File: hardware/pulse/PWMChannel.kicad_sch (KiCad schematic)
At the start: 6 parts, among them J201 WAGO-2065, J202 WAGO-2065, Q201 BSC010N04LS

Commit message: Update parts
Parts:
- C201: footprint Capacitor_SMD:C_0603_1608Metric -> V2_Capacitor_SMD:C_0603; symbol Device:C_Small -> V2_Device:C_0603_0u1; Manufacturer (none) -> TDK; Mouser (none) -> 810-CGA3E2X7R1H104MA; Product (none) -> CGA3E2X7R1H104M080AA
- D201: footprint Diode_SMD:D_SOD-123F -> V2_Diode_SMD:D_SOD-123F; Manufacturer (none) -> onsemi; Mouser (none) -> 512-S310FA; Product (none) -> S310FA
- D202: LCSC (none) -> C965555; Manufacturer (none) -> Worldsemi; Product (none) -> WS2812B-2020
- J201, J202: value WAGO-2065 -> WAGO 2065-100; Manufacturer (none) -> WAGO; Product (none) -> 2065-100/998-403
- Q201: Manufacturer (none) -> Infineon Technologies; Mouser (none) -> 726-BSC010N04LS; Product (none) -> BSC010N04LS
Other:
- moved on the sheet: C201, D201, D202, J201, J202, Q201

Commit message: Refresh
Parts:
- Q201: Polarity (none) -> N; Rating (none) -> 40V
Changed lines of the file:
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@@
-			)
-		)
-		(property "Sim.Pin" ""
-			(at 135.89 93.98 90)
-			(effects
-				(font
-					(size 1.27 1.27)
-				)
-				(hide yes)
 			)
 		)
@@
 		(property "Product" "S310FA"
 			(at 123.19 93.98 0)
-			(effects
-				(font
-					(size 1.27 1.27)
-				)
-				(hide yes)
-			)
-		)
-		(property "Sim.Enable" ""
-			(at 135.89 93.98 90)
 			(effects
 				(font
@@
 			)
 		)
-		(property "Sim.Pin" ""
-			(at 123.19 93.98 0)
-			(effects
-				(font
-					(size 1.27 1.27)
-				)
-				(hide yes)
-			)
-		)
 		(property "Manufacturer" "TDK"
 			(at 123.19 109.22 0)
@@
 		(property "Product" "CGA3E2X7R1H104M080AA"
 			(at 123.19 111.76 0)
-			(effects
-				(font
-					(size 1.27 1.27)
-				)
-				(hide yes)
-			)
-		)
-		(property "Sim.Enable" ""
-			(at 123.19 93.98 0)
 			(effects
 				(font
@@
 			)
 		)
-		(property "Sim.Pin" ""
-			(at 120.65 101.6 0)
-			(effects
-				(font
-					(size 1.27 1.27)
-				)
-				(hide yes)
-			)
-		)
 		(property "Product" "BSC010N04LS"
 			(at 120.65 121.92 0)
@@
 			)
 		)
-		(property "Sim.Enable" ""
-			(at 120.65 101.6 0)
+		(property "Rating" "40V"
+			(at 120.65 121.92 0)
+			(effects
+				(font
+					(size 1.27 1.27)
+				)
+				(hide yes)
+			)
+		)
+		(property "Polarity" "N"
+			(at 120.65 119.38 0)
 			(effects
 				(font
@@
 			)
 		)
-		(property "Sim.Pin" ""
-			(at 148.59 130.81 0)
-			(effects
-				(font
-					(size 1.27 1.27)
-				)
-				(hide yes)
-			)
-		)
-		(property "Sim.Enable" ""
-			(at 148.59 130.81 0)
-			(effects
-				(font
-					(size 1.27 1.27)
-				)
-				(hide yes)
-			)
-		)
 		(pin "1"
 		)
@@
 			)
 		)
-		(property "Sim.Pin" ""
-			(at 165.1 91.44 0)
-			(effects
-				(font
-					(size 1.27 1.27)
-				)
-				(hide yes)
-			)
-		)
-		(property "Sim.Enable" ""
-			(at 165.1 91.44 0)
-			(effects
-				(font
-					(size 1.27 1.27)
-				)
-				(hide yes)
-			)
-		)
 		(pin "1"
 		)
@@
 			(effects
 				(font
-					(size 1.27 1.27)
-				)
-				(hide yes)
-			)
-		)
-		(property "Sim.Pin" ""
-			(at 165.1 96.52 0)
-			(effects
-				(font
-					(size 1.27 1.27)
-				)
-				(hide yes)
-			)
-		)
-		(property "Sim.Enable" ""
-			(at 165.1 96.52 0)
-			(effects
-				(font

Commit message: Update library
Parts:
- C201: Rating (none) -> 50V
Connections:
- net +24V renamed +28V
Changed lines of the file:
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@@
+			)
+		)
+		(property "Rating" "50V"
+			(at 123.19 116.84 0)
+			(effects
+				(font
+					(size 1.27 1.27)
+				)
+				(hide yes)
 			)
 		)
@@
 			)
 		)
-		(property "Description" "Power symbol creates a global label with name \"GND\" , ground"
+		(property "Description" ""
 			(at 156.21 132.08 0)
 			(effects
@@
 	)
 	(symbol
-		(lib_id "V2_power:+24V")
+		(lib_id "V2_power:+28V")
 		(at 160.02 91.44 0)
 		(unit 1)
@@
 			)
 		)
-		(property "Value" "+24V"
+		(property "Value" "+28V"
 			(at 160.02 86.995 0)
 			(effects
@@
 			)
 		)
-		(property "Description" "Power symbol creates a global label with name \"+24V\""
+		(property "Description" ""
 			(at 160.02 91.44 0)
 			(effects
@@
 			)
 		)
-		(property "Description" "Power symbol creates a global label with name \"GND\" , ground"
+		(property "Description" ""
 			(at 123.19 106.68 0)
 			(effects
@@
 			)
 		)
-		(property "Description" "Power symbol creates a global label with name \"+5V\""
+		(property "Description" ""
 			(at 156.21 127 0)
 			(effects

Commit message: Update Library
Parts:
- C201: symbol V2_Device:C_0603_0u1 -> V2_Capacitor:0603_0u1
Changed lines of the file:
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@@
 	)
 	(symbol
-		(lib_id "V2_Device:C_0603_0u1")
+		(lib_id "V2_Capacitor:0603_0u1")
 		(at 123.19 93.98 0)
 		(unit 1)

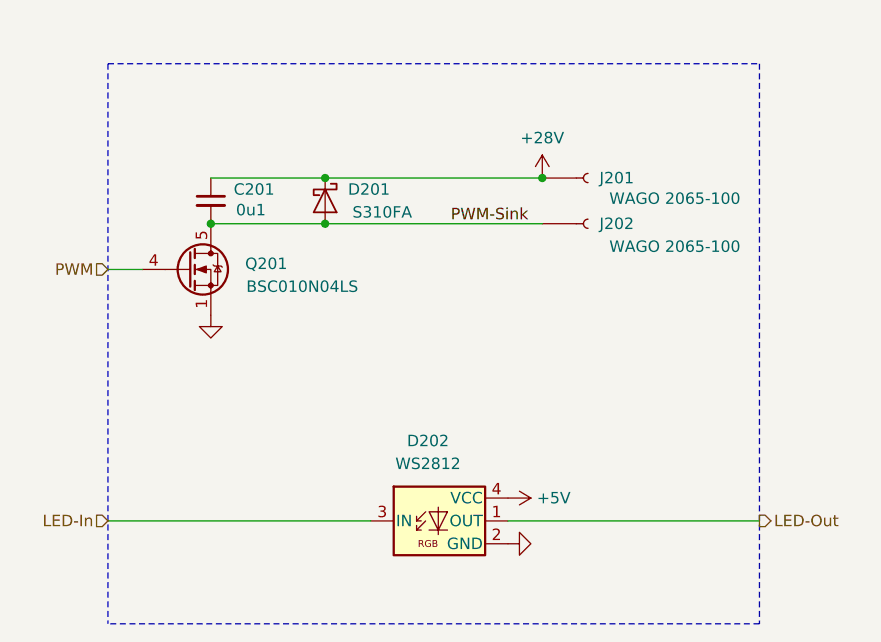
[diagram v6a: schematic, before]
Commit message: Replace diode
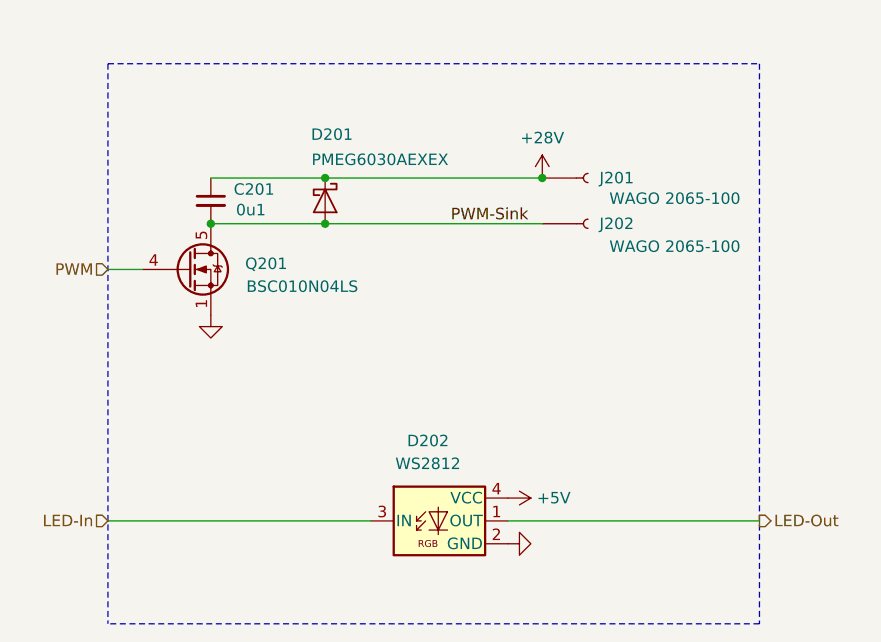
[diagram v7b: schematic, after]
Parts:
- D201: value S310FA -> PMEG6030AEXEX; footprint V2_Diode_SMD:D_SOD-123F -> V2_Diode_SMD:D_SOD-123HP; symbol V2_Diode:S310FA -> V2_Diode:PMEG6030AEXEX; Manufacturer onsemi -> Nexperia; Mouser 512-S310FA -> 771-PMEG6030AEXEX; Product S310FA -> PMEG6030AEXEX
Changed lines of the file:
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@@
 	(title_block
 		(title "Solenoid Channel")
-		(date "2026-01-13")
-		(rev "2")
+		(date "2026-03-11")
+		(rev "2026-03-11")
 		(company "Power MOSFET + RGB LED")
 	)
@@
 	)
 	(symbol
-		(lib_id "V2_Diode:S310FA")
+		(lib_id "V2_Diode:PMEG6030AEXEX")
 		(at 135.89 93.98 270)
 		(unit 1)
@@
 		(dnp no)
 		(property "Reference" "D201"
-			(at 138.43 92.71 90)
-			(effects
-				(font
-					(size 1.27 1.27)
-				)
-				(justify left)
-			)
-		)
-		(property "Value" "S310FA"
-			(at 142.24 95.25 90)
-			(effects
-				(font
-					(size 1.27 1.27)
-				)
-			)
-		)
-		(property "Footprint" "V2_Diode_SMD:D_SOD-123F"
-			(at 128.905 93.98 0)
+			(at 136.652 86.614 90)
+			(effects
+				(font
+					(size 1.27 1.27)
+				)
+			)
+		)
+		(property "Value" "PMEG6030AEXEX"
+			(at 141.986 89.408 90)
+			(effects
+				(font
+					(size 1.27 1.27)
+				)
+			)
+		)
+		(property "Footprint" "V2_Diode_SMD:D_SOD-123HP"
+			(at 128.27 93.98 0)
 			(effects
 				(font
@@
 			)
 		)
-		(property "Mouser" "512-S310FA"
+		(property "Mouser" "771-PMEG6030AEXEX"
+			(at 120.65 93.98 0)
+			(show_name yes)
+			(effects
+				(font
+					(size 1.27 1.27)
+				)
+				(hide yes)
+			)
+		)
+		(property "Manufacturer" "Nexperia"
 			(at 125.73 93.98 0)
-			(effects
-				(font
-					(size 1.27 1.27)
-				)
-				(hide yes)
-			)
-		)
-		(property "Manufacturer" "onsemi"
-			(at 125.73 93.98 0)
-			(effects
-				(font
-					(size 1.27 1.27)
-				)
-				(hide yes)
-			)
-		)
-		(property "Product" "S310FA"
+			(show_name yes)
+			(effects
+				(font
+					(size 1.27 1.27)
+				)
+				(hide yes)
+			)
+		)
+		(property "Product" "PMEG6030AEXEX"
 			(at 123.19 93.98 0)
+			(show_name yes)
 			(effects
 				(font
@@
 			)
 		)
-		(property "Description" "Unpolarized capacitor, small symbol"
+		(property "Description" ""
 			(at 123.19 107.442 0)
 			(effects

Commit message: Update ESD suppressor
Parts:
- D201: Rating (none) -> 60V
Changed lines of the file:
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@@
+			)
+		)
+		(property "Rating" "60V"
+			(at 118.11 93.98 0)
+			(effects
+				(font
+					(size 1.27 1.27)
+				)
+				(hide yes)
 			)
 		)
